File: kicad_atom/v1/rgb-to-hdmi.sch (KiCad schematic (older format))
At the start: 49 parts, among them J1 Conn_02x05_Odd_Even, J2 Conn_01x20, J3 Conn_01x20, J4 Conn_01x03, J5 Conn_02x20_Odd_Even, SW1 SW_Push_Dual, SW2 SW_Push_Dual, SW3 SW_Push_Dual, U1 74LVC1G66, U2 LM319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

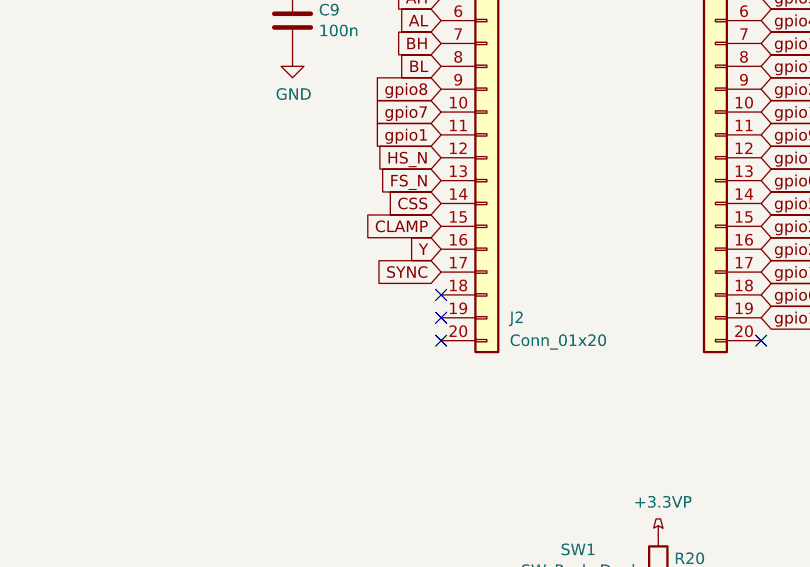
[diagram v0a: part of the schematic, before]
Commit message: Atom PCB: Prototype (just about complete)
Change-Id: Iee45754a64bc2e643c024d613505a408e311c64b
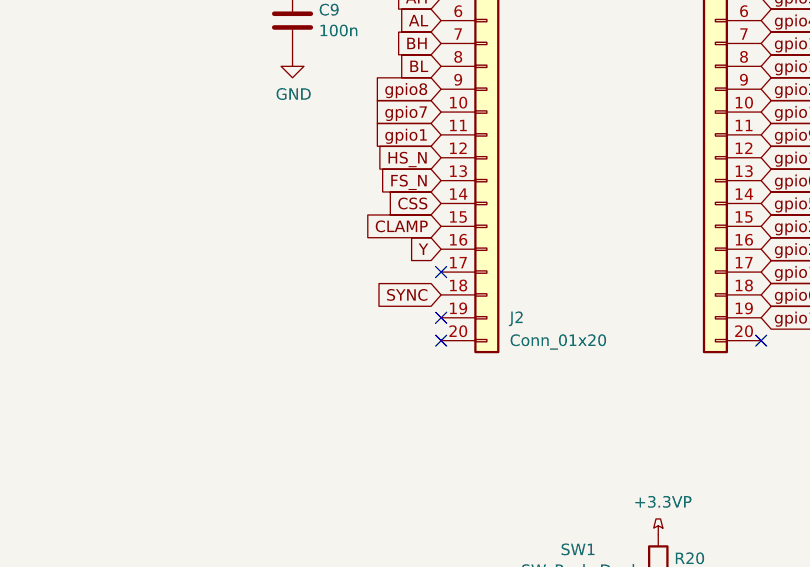
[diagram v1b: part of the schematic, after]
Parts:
- C1, C10, C11, C12, C2, C3, C5, C6, C7, C8, C9: footprint Capacitor_THT:C_Rect_L7.0mm_W2.5mm_P5.00mm -> local:C_Rect_L7.0mm_W2.5mm_P5.00mm
- C13, C4: footprint Capacitor_THT:CP_Radial_D5.0mm_P2.50mm -> local:CP_Radial_D5.0mm_P2.50mm
- J1: footprint Connector_PinHeader_2.54mm:PinHeader_2x05_P2.54mm_Vertical -> local:PinHeader_2x05_P2.54mm_Vertical
- J2, J3: footprint Connector_PinSocket_2.54mm:PinSocket_1x20_P2.54mm_Vertical -> local:PinSocket_1x20_P2.54mm_Vertical
- J4: footprint Connector_PinHeader_2.54mm:PinHeader_1x03_P2.54mm_Vertical -> local:PinHeader_1x03_P2.54mm_Vertical
- J5: footprint Connector_PinSocket_2.54mm:PinSocket_2x20_P2.54mm_Vertical -> local:PinSocket_2x20_P2.54mm_Vertical
- R1, R10, R11, R12, R13, R14, R15, R16, R17, R18, R19, R2, R20, R21, R22, R3, R4, R5, R6, R7, R8, R9: footprint Resistor_THT:R_Axial_DIN0207_L6.3mm_D2.5mm_P10.16mm_Horizontal -> local:R_Axial_DIN0207_L6.3mm_D2.5mm_P10.16mm_Horizontal
- RV1, RV2: footprint Potentiometer_THT:Potentiometer_Vishay_T73YP_Vertical -> local:Potentiometer_Vishay_T73YP_Vertical
- SW1, SW2, SW3: footprint Button_Switch_THT:SW_TH_Tactile_Omron_B3F-10xx -> local:SW_TH_Tactile_Omron_B3F-10xx
- U2, U3, U4: footprint Package_DIP:DIP-14_W7.62mm_Socket_LongPads -> local:DIP-14_W7.62mm_Socket_LongPads
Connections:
- net SYNC: now also J2.18 (Pin_18); no longer J2.17 (Pin_17)
